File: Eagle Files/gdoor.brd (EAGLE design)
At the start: 73.7 x 30.5 mm, 9 parts

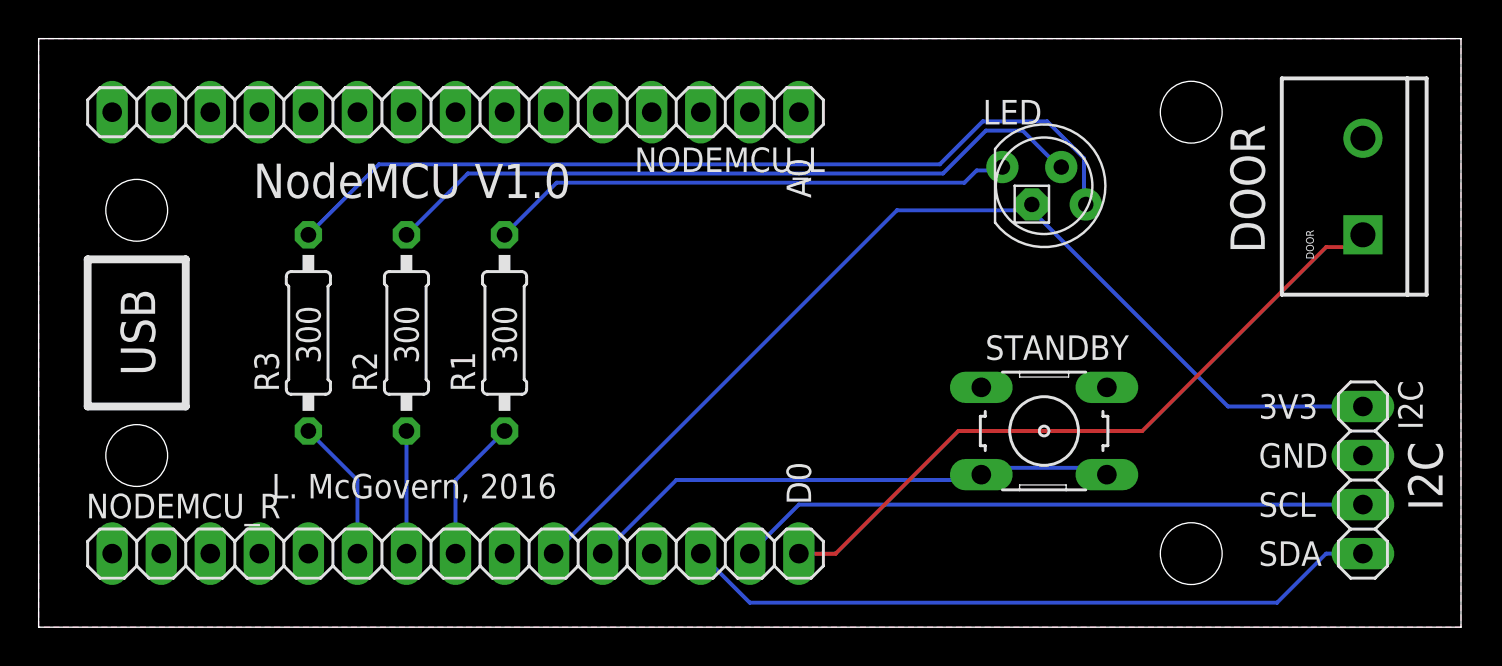
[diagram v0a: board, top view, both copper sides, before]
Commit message: Code and PCB modified for robustness
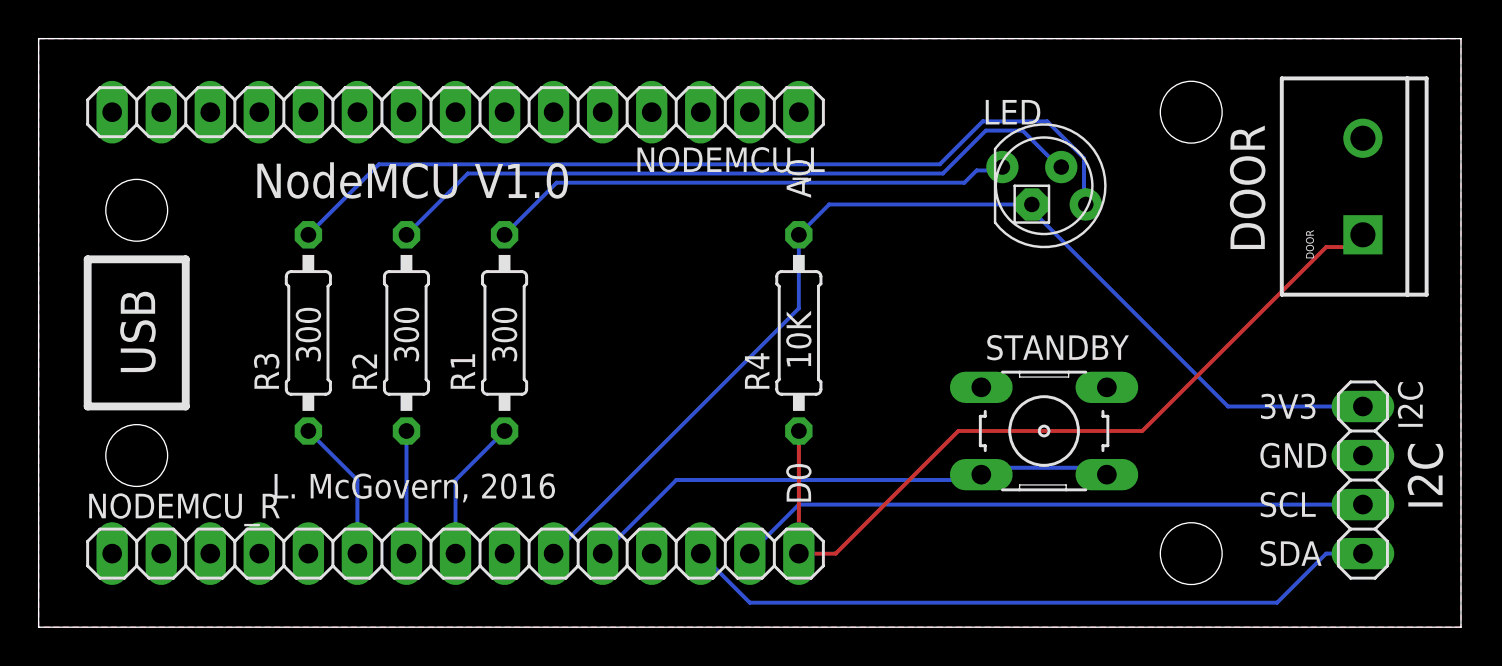
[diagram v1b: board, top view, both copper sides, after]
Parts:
- added R4: 10K, resistor:0207/10
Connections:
- net +3V3: now also R4.2
- net D0: now also R4.1
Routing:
- net D0: track 36.0 -> 42.4 mm
- net +3V3: track 53.8 -> 56.1 mm
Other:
- board text added: "10K"
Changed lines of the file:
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@@
 <?xml version="1.0" encoding="utf-8"?>
 <!DOCTYPE eagle SYSTEM "eagle.dtd">
-<eagle version="7.7.0">
+<eagle version="9.2.2">
 <drawing>
 <settings>
 <setting alwaysvectorfont="no"/>
+<setting keepoldvectorfont="yes"/>
 <setting verticaltext="up"/>
 </settings>
-<grid distance="0.1" unitdist="inch" unit="inch" style="lines" multiple="1" display="yes" altdistance="0.0125" altunitdist="inch" altunit="inch"/>
+<grid distance="0.1" unitdist="inch" unit="inch" style="lines" multiple="1" display="yes" altdistance="0.025" altunitdist="inch" altunit="inch"/>
 <layers>
 <layer number="1" name="Top" color="4" fill="1" visible="yes" active="yes"/>
@@
 <text x="24.765" y="13.6525" size="1.27" layer="21" rot="R90">300</text>
 <wire x1="0" y1="30.48" x2="0" y2="0" width="0" layer="20"/>
+<text x="40.005" y="13.335" size="1.27" layer="21" rot="R90">10K</text>
 </plain>
 <attributes>
@@
 <param name="dpMaxLengthDifference" value="10mm"/>
 <param name="dpGapFactor" value="2.5"/>
-<param name="checkGrid" value="0"/>
 <param name="checkAngle" value="0"/>
 <param name="checkFont" value="1"/>
 <param name="checkRestrict" value="1"/>
+<param name="checkStop" value="0"/>
+<param name="checkValues" value="0"/>
+<param name="checkNames" value="1"/>
+<param name="checkWireStubs" value="1"/>
+<param name="checkPolygonWidth" value="0"/>
 <param name="useDiameter" value="13"/>
 <param name="maxErrors" value="50"/>
@@
 </autorouter>
 <elements>
-<element name="DOOR" library="SparkFun-Connectors" package="SCREWTERMINAL-5MM-2" value="" x="68.58" y="20.32" rot="R90">
+<element name="DOOR" library="SparkFun-Connectors" package="SCREWTERMINAL-5MM-2" value="" x="68.58" y="20.32" smashed="yes" rot="R90">
+<attribute name="NAME" x="66.04" y="19.05" size="0.4064" layer="25" rot="R90"/>
 <attribute name="STOREFRONT_ID" value="PRT-08432" x="68.58" y="20.32" size="1.778" layer="27" rot="R90" display="off"/>
-</element>
-<element name="I2C" library="pinhead" package="1X04" value="" x="68.58" y="7.62" rot="R270"/>
-<element name="NODEMCU_L" library="pinhead" package="1X15" value="" x="21.59" y="26.67" rot="R180"/>
-<element name="NODEMCU_R" library="pinhead" package="1X15" value="" x="21.59" y="3.81"/>
-<element name="R1" library="resistor" package="0207/10" value="300" x="24.13" y="15.24" rot="R90"/>
-<element name="R2" library="resistor" package="0207/10" value="300" x="19.05" y="15.24" rot="R90"/>
-<element name="R3" library="resistor" package="0207/10" value="300" x="13.97" y="15.24" rot="R90"/>
-<element name="STANDBY" library="switch-omron" package="B3F-10XX" value="" x="52.07" y="10.16">
+<attribute name="VALUE" x="67.31" y="19.05" size="0.4064" layer="27" rot="R90"/>
+</element>
+<element name="I2C" library="pinhead" package="1X04" value="" x="68.58" y="7.62" smashed="yes" rot="R270">
+<attribute name="NAME" x="70.4088" y="12.7762" size="1.27" layer="25" ratio="10" rot="R270"/>
+<attribute name="VALUE" x="65.405" y="12.7" size="1.27" layer="27" rot="R270"/>
+</element>
+<element name="NODEMCU_L" library="pinhead" package="1X15" value="" x="21.59" y="26.67" smashed="yes" rot="R180">
+<attribute name="NAME" x="40.7162" y="24.8412" size="1.27" layer="25" ratio="10" rot="R180"/>
+<attribute name="VALUE" x="40.64" y="29.845" size="1.27" layer="27" rot="R180"/>
+</element>
+<element name="NODEMCU_R" library="pinhead" package="1X15" value="" x="21.59" y="3.81" smashed="yes">
+<attribute name="NAME" x="2.4638" y="5.6388" size="1.27" layer="25" ratio="10"/>
+<attribute name="VALUE" x="2.54" y="0.635" size="1.27" layer="27"/>
+</element>
+<element name="R1" library="resistor" package="0207/10" value="300" x="24.13" y="15.24" smashed="yes" rot="R90">
+<attribute name="NAME" x="22.606" y="12.192" size="1.27" layer="25" ratio="10" rot="R90"/>
+<attribute name="VALUE" x="24.765" y="12.9794" size="1.27" layer="27" ratio="10" rot="R90"/>
+</element>
+<element name="R2" library="resistor" package="0207/10" value="300" x="19.05" y="15.24" smashed="yes" rot="R90">
+<attribute name="NAME" x="17.526" y="12.192" size="1.27" layer="25" ratio="10" rot="R90"/>
+<attribute name="VALUE" x="19.685" y="12.9794" size="1.27" layer="27" ratio="10" rot="R90"/>
+</element>
+<element name="R3" library="resistor" package="0207/10" value="300" x="13.97" y="15.24" smashed="yes" rot="R90">
+<attribute name="NAME" x="12.446" y="12.192" size="1.27" layer="25" ratio="10" rot="R90"/>
+<attribute name="VALUE" x="14.605" y="12.9794" size="1.27" layer="27" ratio="10" rot="R90"/>
+</element>
+<element name="STANDBY" library="switch-omron" package="B3F-10XX" value="" x="52.07" y="10.16" smashed="yes">
+<attribute name="MF" value="" x="52.07" y="10.16" size="1.778" layer="27" display="off"/>
+<attribute name="MPN" value="B3F-1000" x="52.07" y="10.16" size="1.778" layer="27" display="off"/>
+<attribute name="NAME" x="49.022" y="13.843" size="1.27" layer="25" ratio="10"/>
 <attribute name="OC_FARNELL" value="176432" x="52.07" y="10.16" size="1.778" layer="27" display="off"/>
 <attribute name="OC_NEWARK" value="36M3542" x="52.07" y="10.16" size="1.778" layer="27" display="off"/>
-<attribute name="MF" value="" x="52.07" y="10.16" size="1.778" layer="27" display="off"/>
-<attribute name="MPN" value="B3F-1000" x="52.07" y="10.16" size="1.778" layer="27" display="off"/>
-</element>
-<element name="LED" library="adafruit" package="LED5MMRGB" value="RGBLED_CA-5MM" x="52.07" y="22.86"/>
+<attribute name="VALUE" x="49.022" y="5.08" size="1.27" layer="27" ratio="10"/>
+</element>
+<element name="LED" library="adafruit" package="LED5MMRGB" value="RGBLED_CA-5MM" x="52.07" y="22.86" smashed="yes">
+<attribute name="NAME" x="48.895" y="26.035" size="1.27" layer="25"/>
+</element>
+<element name="R4" library="resistor" package="0207/10" value="10K" x="39.37" y="15.24" smashed="yes" rot="R90">
+<attribute name="NAME" x="37.846" y="12.192" size="1.27" layer="25" ratio="10" rot="R90"/>
+<attribute name="VALUE" x="40.005" y="12.9794" size="1.27" layer="27" ratio="10" rot="R90"/>
+</element>
 </elements>
 <signals>
@@
 <contactref element="LED" pad="2"/>
 <contactref element="NODEMCU_R" pad="10"/>
-<wire x1="44.45" y1="21.59" x2="26.67" y2="3.81" width="0.2032" layer="16"/>
-<wire x1="51.435" y1="21.59" x2="44.45" y2="21.59" width="0.2032" layer="16"/>
 <wire x1="61.595" y1="11.43" x2="68.58" y2="11.43" width="0.2032" layer="16"/>
 <wire x1="51.435" y1="21.59" x2="61.595" y2="11.43" width="0.2032" layer="16"/>
 <wire x1="51.435" y1="21.59" x2="51.435" y2="21.8916" width="0.2032" layer="16"/>
+<contactref element="R4" pad="2"/>
+<wire x1="39.37" y1="20.32" x2="40.9416" y2="21.8916" width="0.2032" layer="16"/>
+<wire x1="40.9416" y1="21.8916" x2="51.435" y2="21.8916" width="0.2032" layer="16"/>
+<wire x1="26.67" y1="3.81" x2="39.37" y2="16.51" width="0.2032" layer="16"/>
+<wire x1="39.37" y1="16.51" x2="39.37" y2="20.32" width="0.2032" layer="16"/>
 </signal>
 <signal name="GND">
@@
 <wire x1="67.945" y1="19.685" x2="66.675" y2="19.685" width="0.2032" layer="1"/>
 <wire x1="68.58" y1="20.32" x2="67.945" y2="19.685" width="0.2032" layer="1"/>
+<contactref element="R4" pad="1"/>
+<wire x1="39.37" y1="3.81" x2="39.37" y2="10.16" width="0.2032" layer="1"/>
 </signal>
 <signal name="SCL">
@@
 </signal>
 </signals>
+<mfgpreviewcolors>
+<mfgpreviewcolor name="soldermaskcolor" color="0xC8008000"/>
+<mfgpreviewcolor name="silkscreencolor" color="0xFFFEFEFE"/>
+<mfgpreviewcolor name="backgroundcolor" color="0xFF282828"/>
+<mfgpreviewcolor name="coppercolor" color="0xFFFFBF00"/>
+<mfgpreviewcolor name="substratecolor" color="0xFF786E46"/>
+</mfgpreviewcolors>
 </board>
 </drawing>
